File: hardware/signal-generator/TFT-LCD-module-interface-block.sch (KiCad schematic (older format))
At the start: 5 parts

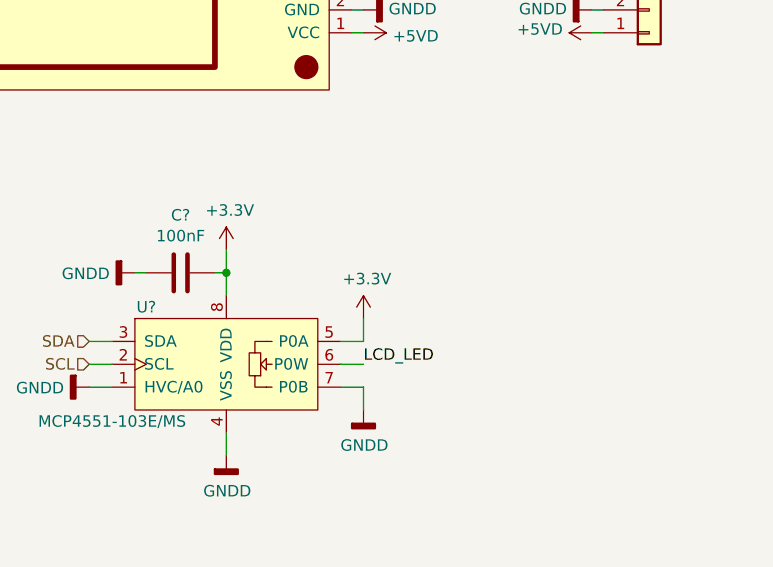
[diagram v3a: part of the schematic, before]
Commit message: [Signal Generator] Power LCD BL control digital POT from +5VD
The MCP4551 BL control POT is now powered from +5VD. Its terminals are
still connected to +3.3VD and GNDD.

Additionally, a jumper has been added which shorts the +3.3VD rail to
the LCD BL control on the LCD module (MSP3218). If this connection is
shorted, the LCD will always be on at full brightness.
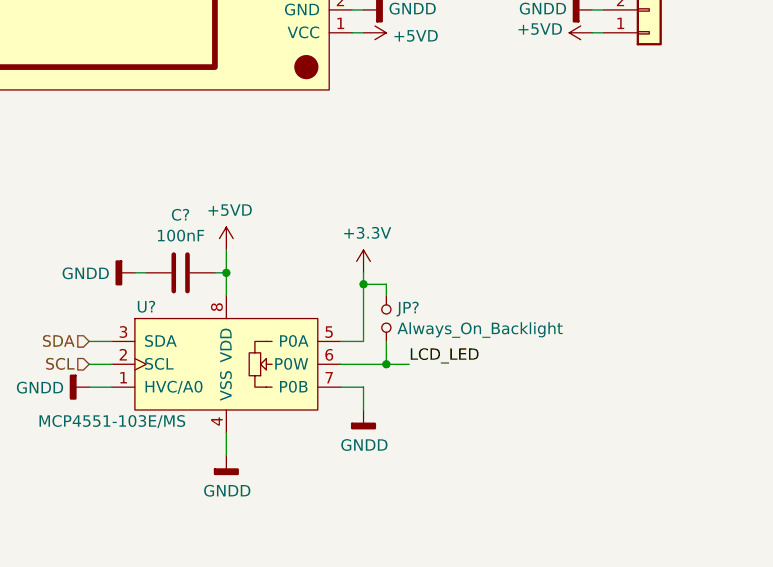
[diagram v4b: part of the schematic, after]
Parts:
- added JP?: Always_On_Backlight, symbol Device:Jumper_NO_Small
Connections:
- net +3V3: now also JP?.1; no longer C?.1, U?.8 (VDD)
- net +5VD: now also C?.1, U?.8 (VDD)
- net LCD_LED: now also JP?.2
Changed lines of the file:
@@
 	0    1    1    0
 $EndComp
-$Comp
-L power:+3.3V #PWR?
-U 1 1 5DF8DC94
-P 6500 4000
-AR Path="/5DF8DC94" Ref="#PWR?"  Part="1"
-AR Path="/5DF89F54/5DF8DC94" Ref="#PWR0223"  Part="1"
-F 0 "#PWR0223" H 6500 3850 50  0001 C CNN
-F 1 "+3.3V" H 6515 4173 50  0000 C CNN
-F 2 "" H 6500 4000 50  0001 C CNN
-F 3 "" H 6500 4000 50  0001 C CNN
-	1    6500 4000
-	1    0    0    -1
-$EndComp
 Wire Wire Line
 	7000 4400 7100 4400
-Wire Wire Line
-	7100 4400 7100 4300
 $Comp
 L power:+3.3V #PWR?
 U 1 1 5DF8DC9C
-P 7100 4300
+P 7100 4100
 AR Path="/5DF8DC9C" Ref="#PWR?"  Part="1"
 AR Path="/5DF89F54/5DF8DC9C" Ref="#PWR0224"  Part="1"
-F 0 "#PWR0224" H 7100 4150 50  0001 C CNN
-F 1 "+3.3V" H 7115 4473 50  0000 C CNN
-F 2 "" H 7100 4300 50  0001 C CNN
-F 3 "" H 7100 4300 50  0001 C CNN
-	1    7100 4300
+F 0 "#PWR0224" H 7100 3950 50  0001 C CNN
+F 1 "+3.3V" H 7115 4273 50  0000 C CNN
+F 2 "" H 7100 4100 50  0001 C CNN
+F 3 "" H 7100 4100 50  0001 C CNN
+	1    7100 4100
 	1    0    0    -1
 $EndComp
@@
 	1    0    0    -1
 $EndComp
-Wire Wire Line
-	7000 4500 7100 4500
-Text Label 7100 4500 0    50   ~ 0
+Text Label 7300 4500 0    50   ~ 0
 LCD_LED
 Text Label 7100 2350 0    50   ~ 0
@@
 	0    1    1    0
 $EndComp
+$Comp
+L power:+5VD #PWR?
+U 1 1 5E0A2195
+P 6500 4000
+F 0 "#PWR?" H 6500 3850 50  0001 C CNN
+F 1 "+5VD" H 6515 4173 50  0000 C CNN
+F 2 "" H 6500 4000 50  0001 C CNN
+F 3 "" H 6500 4000 50  0001 C CNN
+	1    6500 4000
+	1    0    0    -1
+$EndComp
+Wire Wire Line
+	7200 4400 7200 4500
+Wire Wire Line
+	7000 4500 7200 4500
+Wire Wire Line
+	7200 4500 7300 4500
+Connection ~ 7200 4500
+$Comp
+L Device:Jumper_NO_Small JP?
+U 1 1 5E0A7E69
+P 7200 4300
+F 0 "JP?" V 7154 4348 50  0000 L CNN
+F 1 "Always_On_Backlight" V 7245 4348 50  0000 L CNN
+F 2 "" H 7200 4300 50  0001 C CNN
+F 3 "~" H 7200 4300 50  0001 C CNN
+	1    7200 4300
+	0    1    1    0
+$EndComp
+Wire Wire Line
+	7200 4200 7200 4150
+Wire Wire Line
+	7200 4150 7100 4150
+Wire Wire Line
+	7100 4150 7100 4400
+Connection ~ 7100 4150
+Wire Wire Line
+	7100 4100 7100 4150
 $EndSCHEMATC
